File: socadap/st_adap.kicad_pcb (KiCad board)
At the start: 2 copper layers, 29 x 24 mm, 5 parts, among them J1 Conn_02x07_Odd_Even, J2 Conn_01x05_Socket, J3 Conn_01x05_Socket, J4 Conn_01x05_Socket, J5 Conn_01x03_Socket

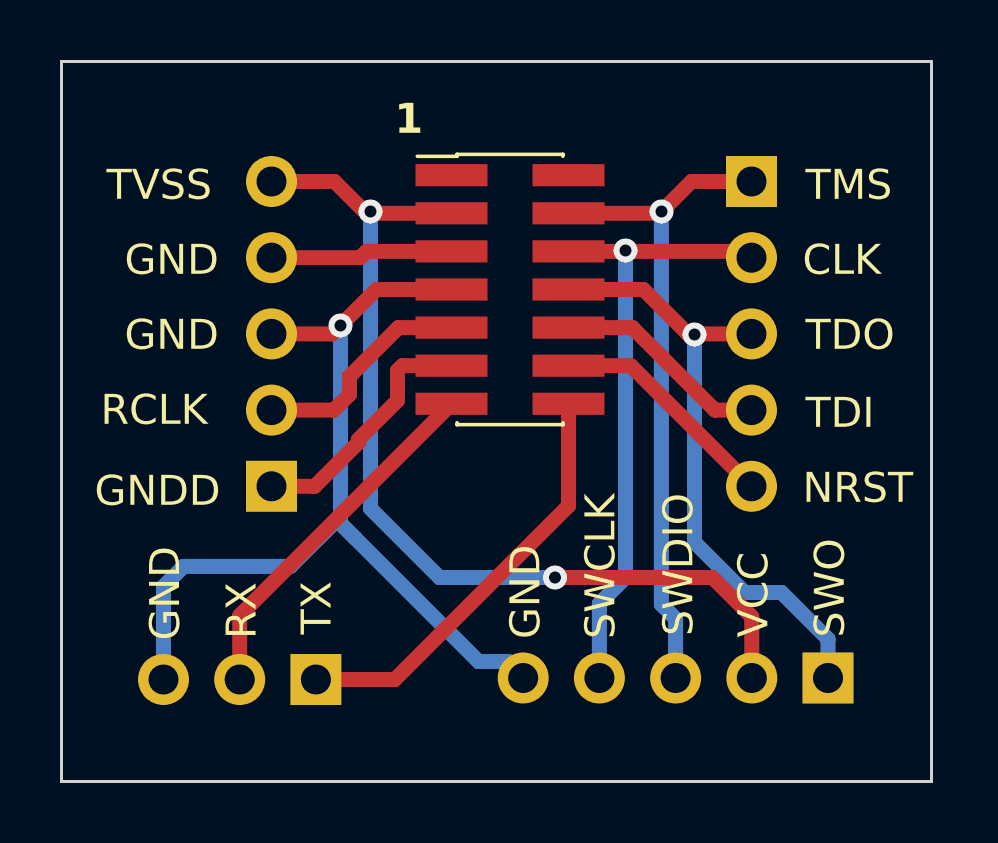
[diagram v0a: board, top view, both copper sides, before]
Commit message: Socket 2x7
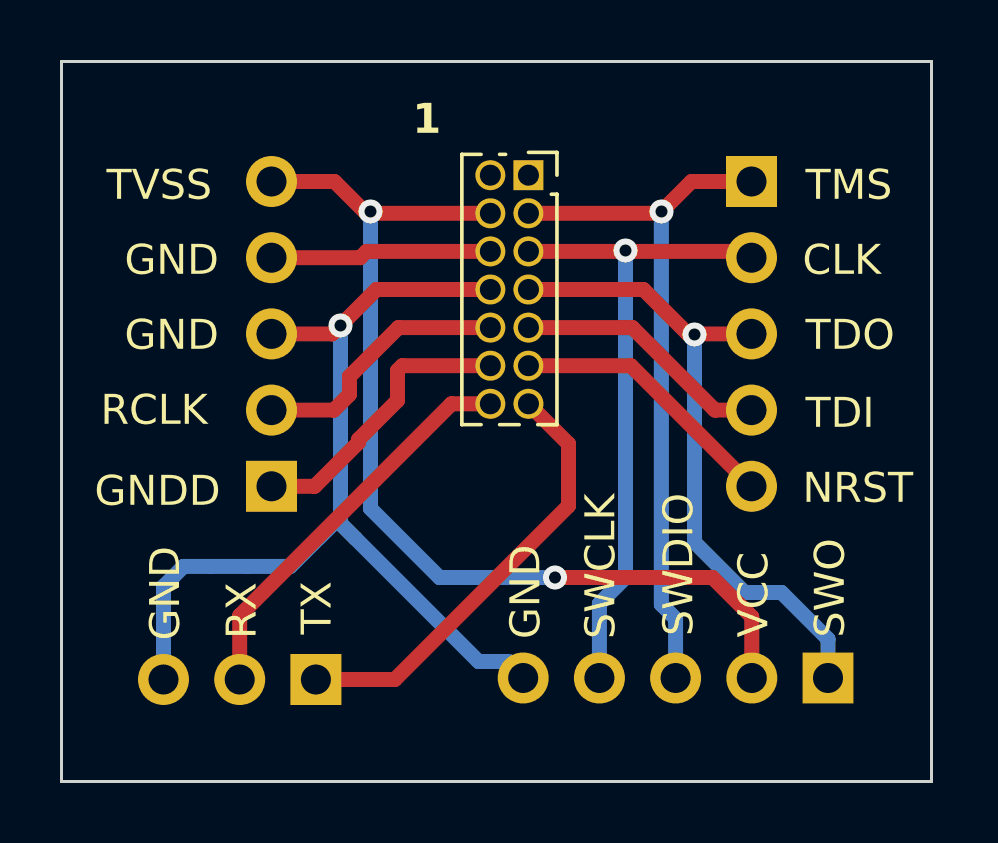
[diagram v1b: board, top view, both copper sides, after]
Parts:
- J1: footprint Connector_PinHeader_1.27mm:PinHeader_2x07_P1.27mm_Vertical_SMD -> Connector_PinSocket_1.27mm:PinSocket_2x07_P1.27mm_Vertical
- moved J1 3.86 mm to (208.6, 97.8)
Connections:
- J1 pad 10: /T_JTDI/NC -> /T_JRCLK
- J1 pad 11: /GNDDETECT -> /T_NRST
- J1 pad 12: /T_NRST -> /GNDDETECT
- J1 pad 13: /T_VCP_RX -> /T_VCP_TX
- J1 pad 14: /T_VCP_TX -> /T_VCP_RX
- J1 pad 3: /T_VCC -> /T_JTMS/T_SWDIO
- J1 pad 4: /T_JTMS/T_SWDIO -> /T_VCC
- J1 pad 5: /GND1 -> /T_JCLK/T_SWCLK
- J1 pad 6: /T_JCLK/T_SWCLK -> /GND1
- J1 pad 7: /GND2 -> /T_JTDO/T_SWO
- J1 pad 8: /T_JTDO/T_SWO -> /GND2
- J1 pad 9: /T_JRCLK -> /T_JTDI/NC
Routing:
- net /T_NRST: track 7.77 -> 9.10 mm
- net /T_JTMS/T_SWDIO: track 22.3 -> 23.6 mm
- net /T_JTDO/T_SWO: track 20.7 -> 22.1 mm
- net /T_JCLK/T_SWCLK: track 20.8 -> 22.1 mm
- net /T_JTDI/NC: track 7.24 -> 8.57 mm
- net /T_VCP_RX: track 12.1 -> 13.4 mm
- net /T_VCC: track 32.6 -> 33.9 mm
- net /T_JRCLK: track 7.49 -> 8.79 mm
- net /GNDDETECT: track 8.31 -> 9.60 mm
- net /GND2: track 33.4 -> 34.7 mm
- net /GND1: track 6.09 -> 7.38 mm
- net /T_VCP_TX: track 14.2 -> 14.8 mm
